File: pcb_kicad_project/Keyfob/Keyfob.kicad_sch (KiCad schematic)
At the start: 17 parts, among them J1 Conn_02x04_Odd_Even, SW1 SW_Push, SW2 SW_Push

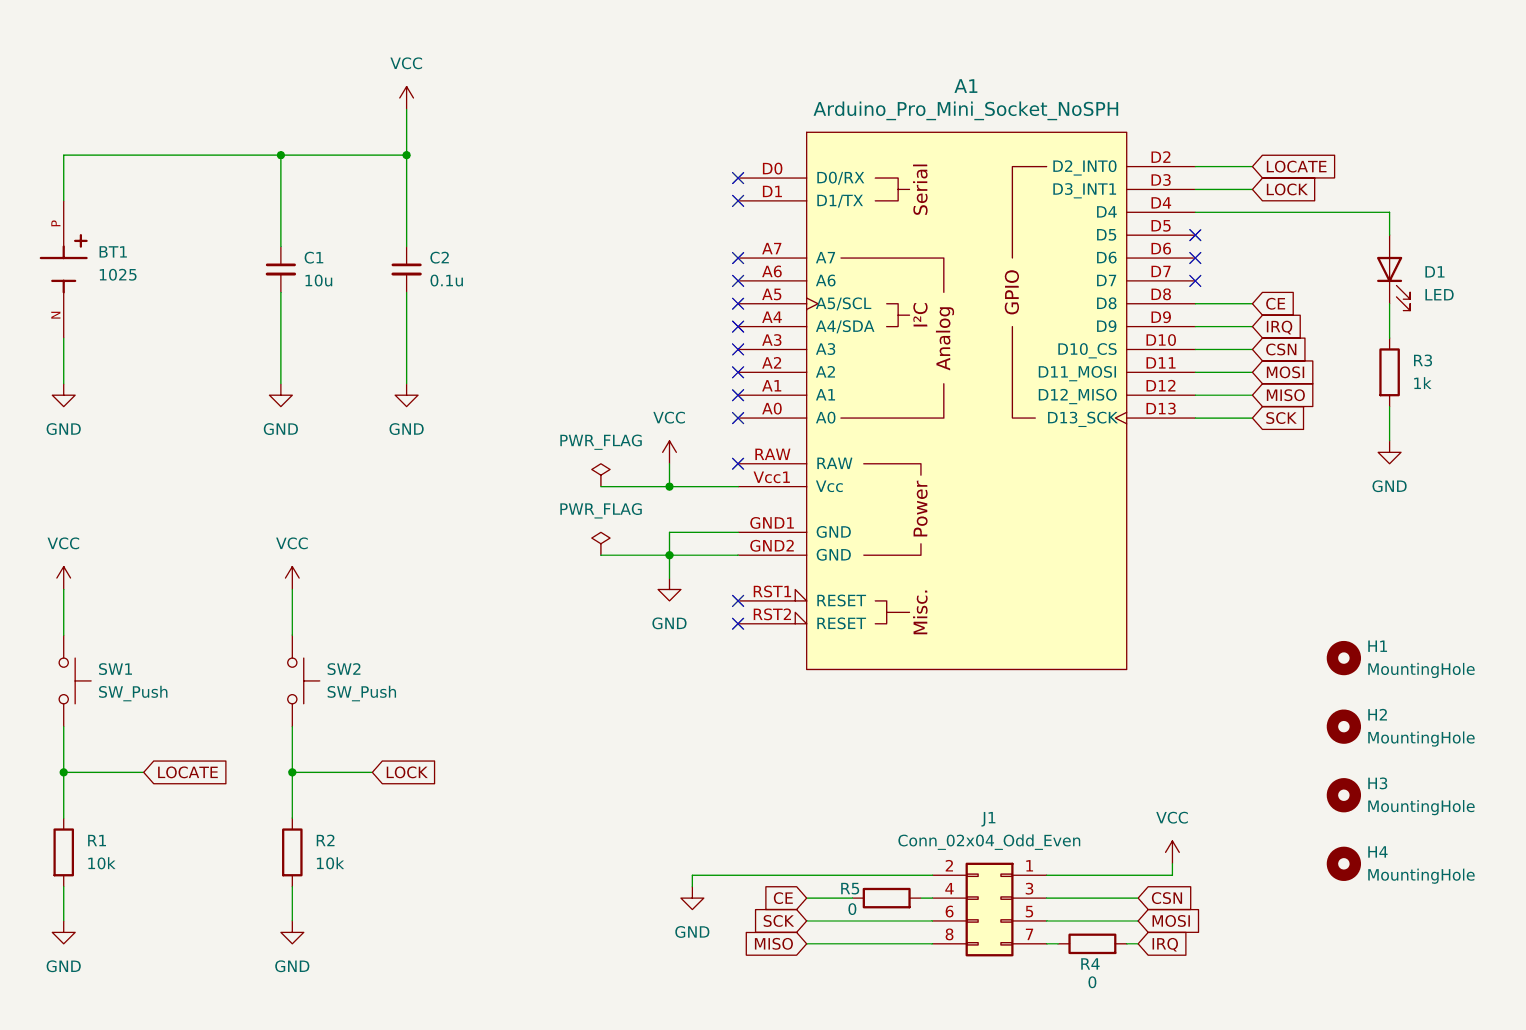
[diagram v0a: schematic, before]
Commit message: update schematic
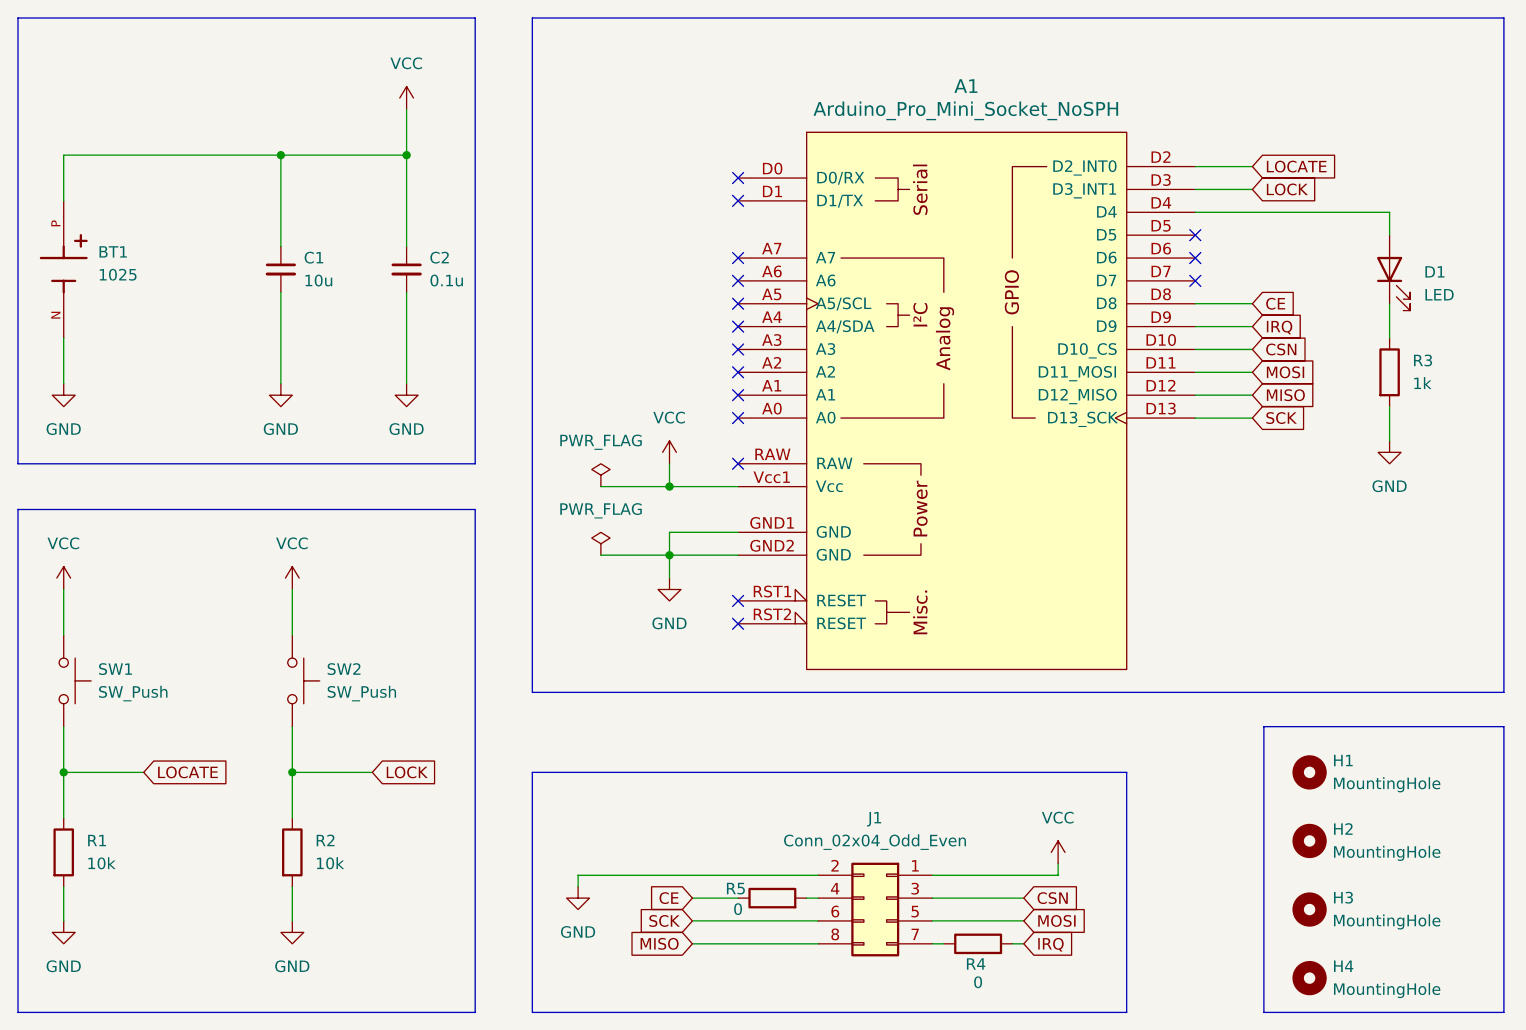
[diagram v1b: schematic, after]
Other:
- moved on the sheet: H1, H2, H3, H4, J1, R4, R5
